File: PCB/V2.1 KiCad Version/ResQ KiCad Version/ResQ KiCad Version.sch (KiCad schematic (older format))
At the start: 8 parts, among them J1 Spare 1, J2 Spare 2, J3 OLED, J4 SD Card, J5 GPS, U1 WeMos_D1_mini

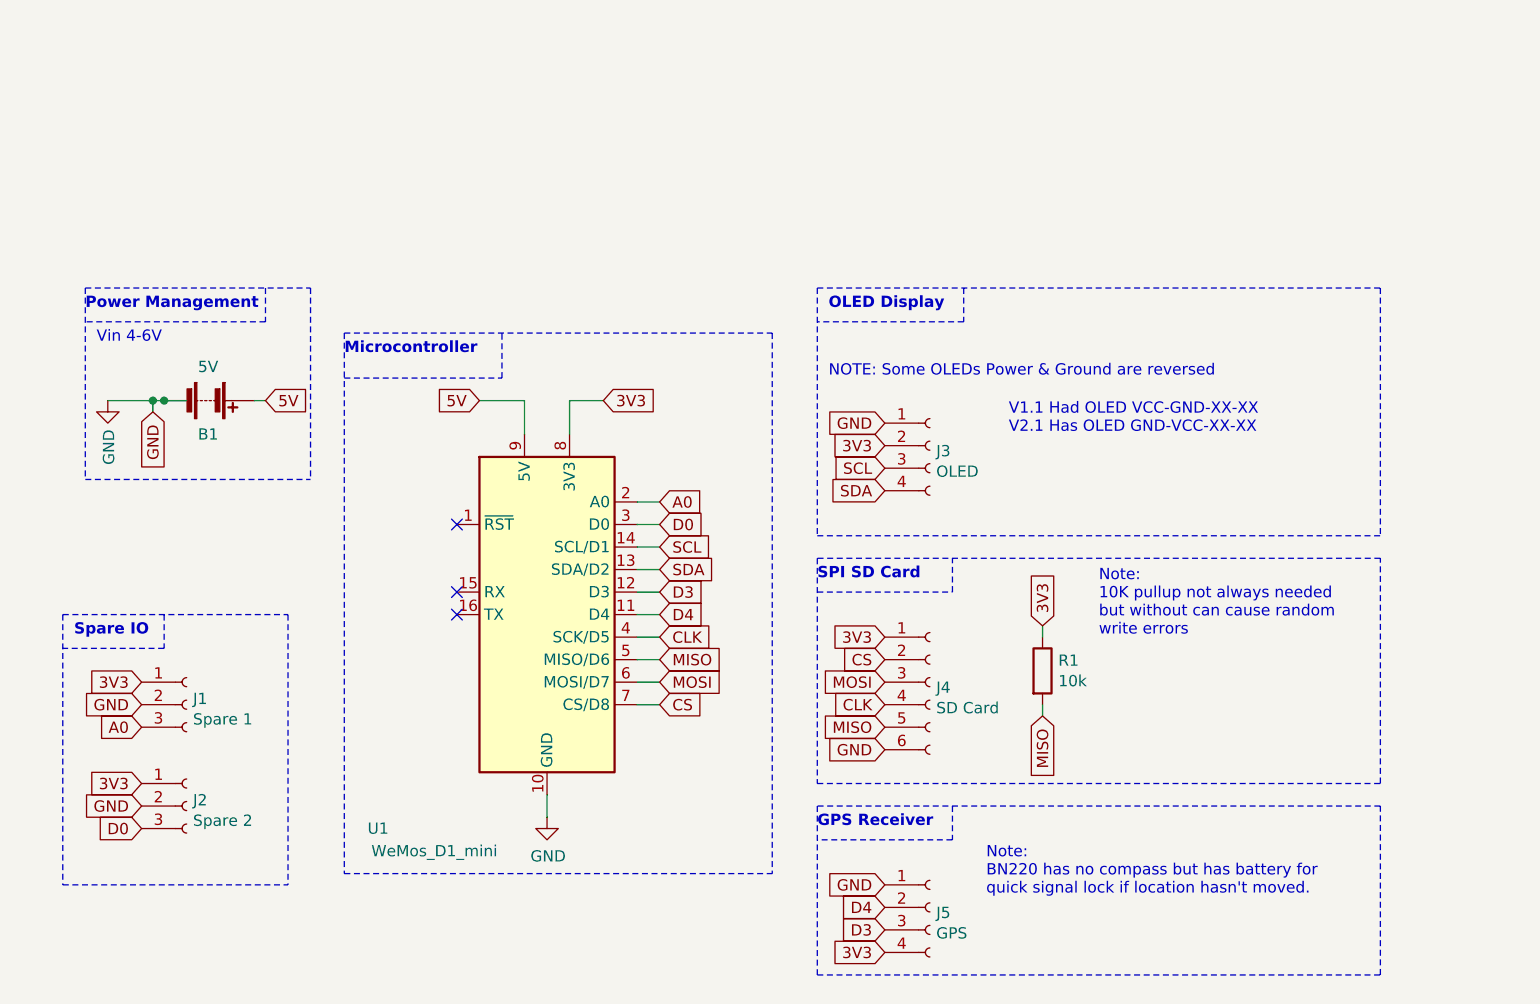
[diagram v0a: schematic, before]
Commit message: Telemetry radio added
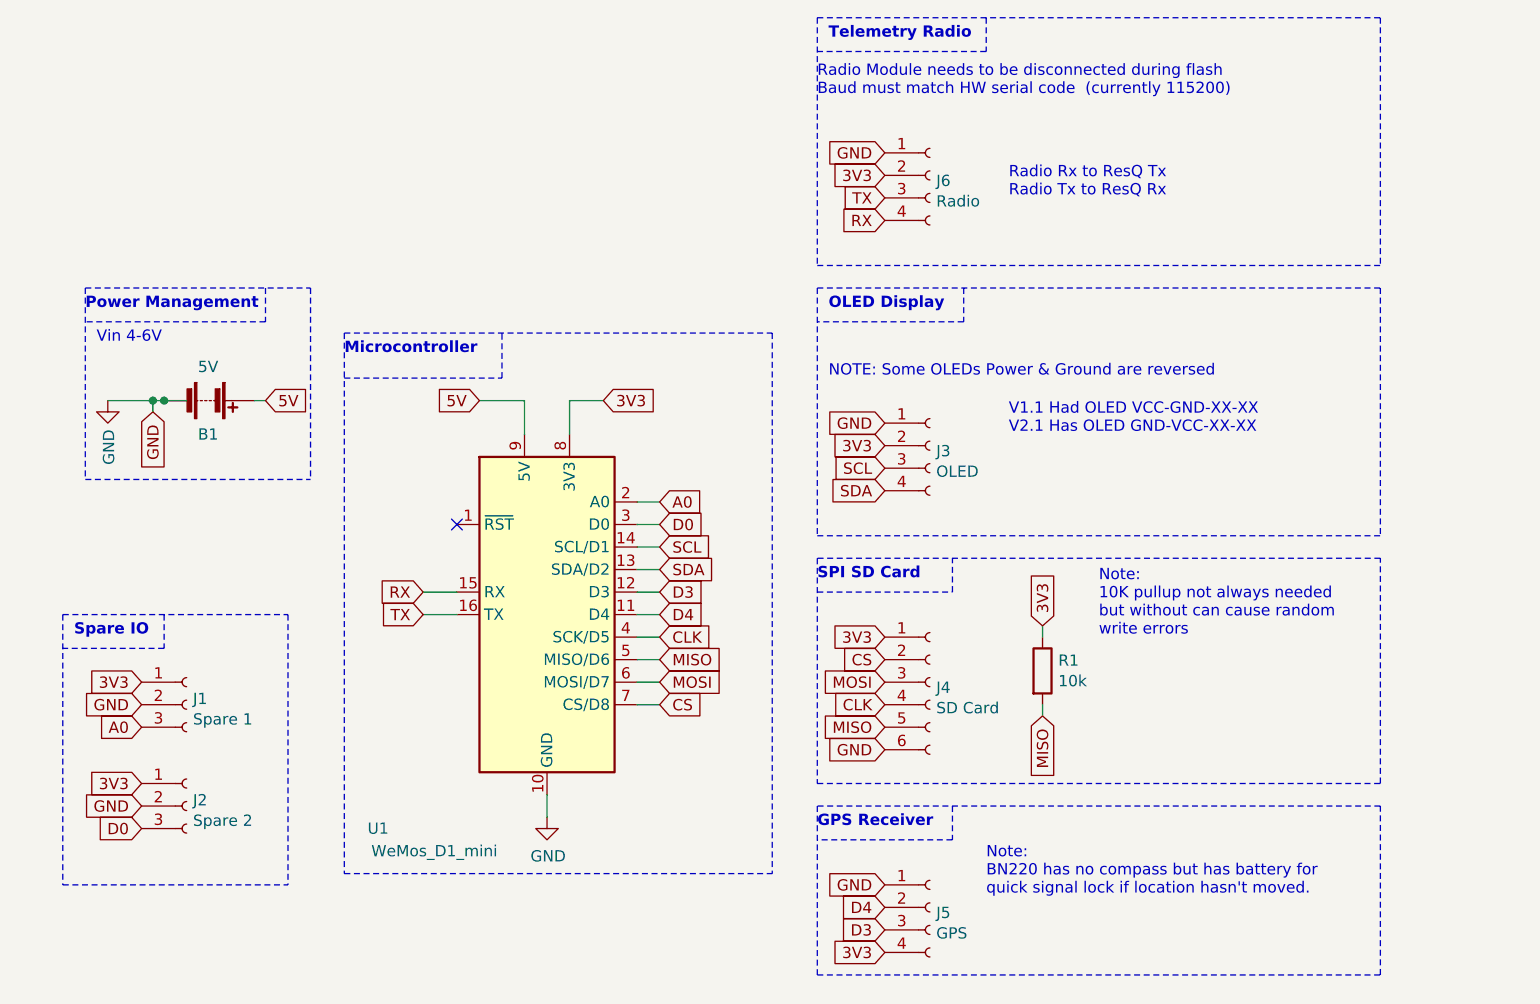
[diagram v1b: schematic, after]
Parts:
- added J6: Radio, Connector_PinSocket_2.54mm:PinSocket_1x04_P2.54mm_Vertical, symbol Connector:Conn_01x04_Female
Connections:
- net labels added: RX, TX
- wire segments 22 -> 24
- no-connect marks 3 -> 1
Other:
- note added: "Radio Module needs to be disconnected during flash \nBaud must match HW serial code (currently 115200)"
- note added: "Radio Rx to ResQ Tx\nRadio Tx to ResQ Rx"
- note added: "Telemetry Radio"
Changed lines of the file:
@@
 Text GLabel 5200 5100 0    50   Input ~ 0
 3V3
-NoConn ~ 6600 4800
-NoConn ~ 6600 4700
 NoConn ~ 6600 4400
 Text GLabel 7500 4700 2    50   Input ~ 0
@@
 	1    0    0    -1
 $EndComp
-Wire Wire Line
-	7000 5600 7000 5700
 Text GLabel 8500 4050 0    50   Input ~ 0
 3V3
@@
 Text Notes 8950 6050 0    50   ~ 0
 Note:\nBN220 has no compass but has battery for \nquick signal lock if location hasn't moved.
-$Comp
-L MCU_Module:WeMos_D1_mini U1
-U 1 1 5F31691B
-P 7000 4800
-F 0 "U1" H 6250 3850 50  0000 C CNN
-F 1 "WeMos_D1_mini" H 6500 3750 50  0000 C CNN
-F 2 "Module:WEMOS_D1_mini_light" H 7000 3650 50  0001 C CNN
-F 3 "https://wiki.wemos.cc/products:d1:d1_mini#documentation" H 5150 3650 50  0001 C CNN
-	1    7000 4800
-	1    0    0    -1
-$EndComp
 Text GLabel 5200 5550 0    50   Input ~ 0
 3V3
@@
 Wire Wire Line
 	7100 3850 7250 3850
+Wire Notes Line
+	8200 2150 8200 3250
+$Comp
+L Connector:Conn_01x04_Female J6
+U 1 1 5F3AE78D
+P 8700 2850
+F 0 "J6" H 8728 2826 50  0000 L CNN
+F 1 "Radio" H 8728 2735 50  0000 L CNN
+F 2 "Connector_PinSocket_2.54mm:PinSocket_1x04_P2.54mm_Vertical" H 8700 2850 50  0001 C CNN
+F 3 "~" H 8700 2850 50  0001 C CNN
+	1    8700 2850
+	1    0    0    -1
+$EndComp
+Text GLabel 8500 2750 0    50   Input ~ 0
+GND
+Text GLabel 8500 2950 0    50   Input ~ 0
+TX
+Text GLabel 8500 3050 0    50   Input ~ 0
+RX
+Text GLabel 8500 2850 0    50   Input ~ 0
+3V3
+Text Notes 8200 2500 0    50   ~ 0
+Radio Module needs to be disconnected during flash \nBaud must match HW serial code  (currently 115200)
+Wire Notes Line
+	10700 2150 10700 3250
+Wire Notes Line
+	8200 2150 10700 2150
+Wire Notes Line
+	8200 3250 10700 3250
+Text Notes 8250 2250 0    50   ~ 10
+Telemetry Radio
+Wire Notes Line
+	8950 2150 8950 2300
+Wire Notes Line
+	8950 2300 8200 2300
+Text GLabel 6450 4800 0    50   Input ~ 0
+TX
+Text GLabel 6450 4700 0    50   Input ~ 0
+RX
+Wire Wire Line
+	7000 5600 7000 5700
+$Comp
+L MCU_Module:WeMos_D1_mini U1
+U 1 1 5F31691B
+P 7000 4800
+F 0 "U1" H 6250 3850 50  0000 C CNN
+F 1 "WeMos_D1_mini" H 6500 3750 50  0000 C CNN
+F 2 "Module:WEMOS_D1_mini_light" H 7000 3650 50  0001 C CNN
+F 3 "https://wiki.wemos.cc/products:d1:d1_mini#documentation" H 5150 3650 50  0001 C CNN
+	1    7000 4800
+	1    0    0    -1
+$EndComp
+Wire Wire Line
+	6600 4700 6450 4700
+Wire Wire Line
+	6600 4800 6450 4800
+Text Notes 9050 2950 0    50   ~ 0
+Radio Rx to ResQ Tx\nRadio Tx to ResQ Rx
 $EndSCHEMATC

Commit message: Scematic fixes
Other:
- note added: "May add switch input\nto allow toggle between menu\nfunctions"
- note added: "Note:\nBN220 has no compass"
- note removed: "Note:\nBN220 has no compass but has battery for \nquick signal lock if location hasn't moved."
- moved on the sheet: B1, J1, J2, J3, J4, J5, J6, R1, U1

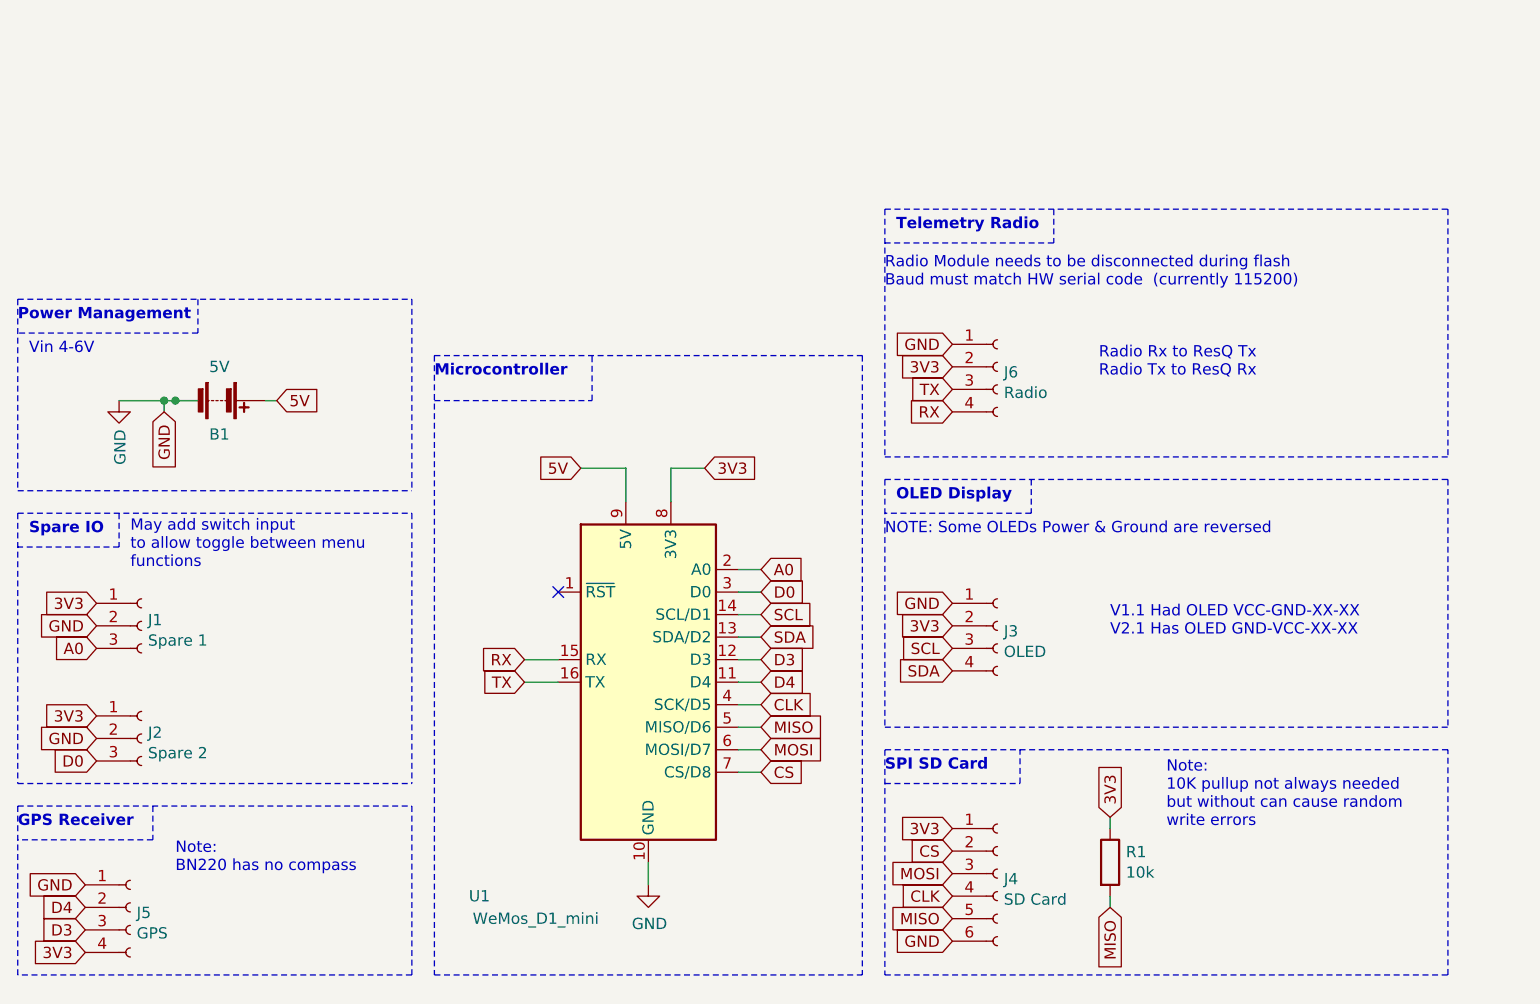
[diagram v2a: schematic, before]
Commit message: Camera Module added
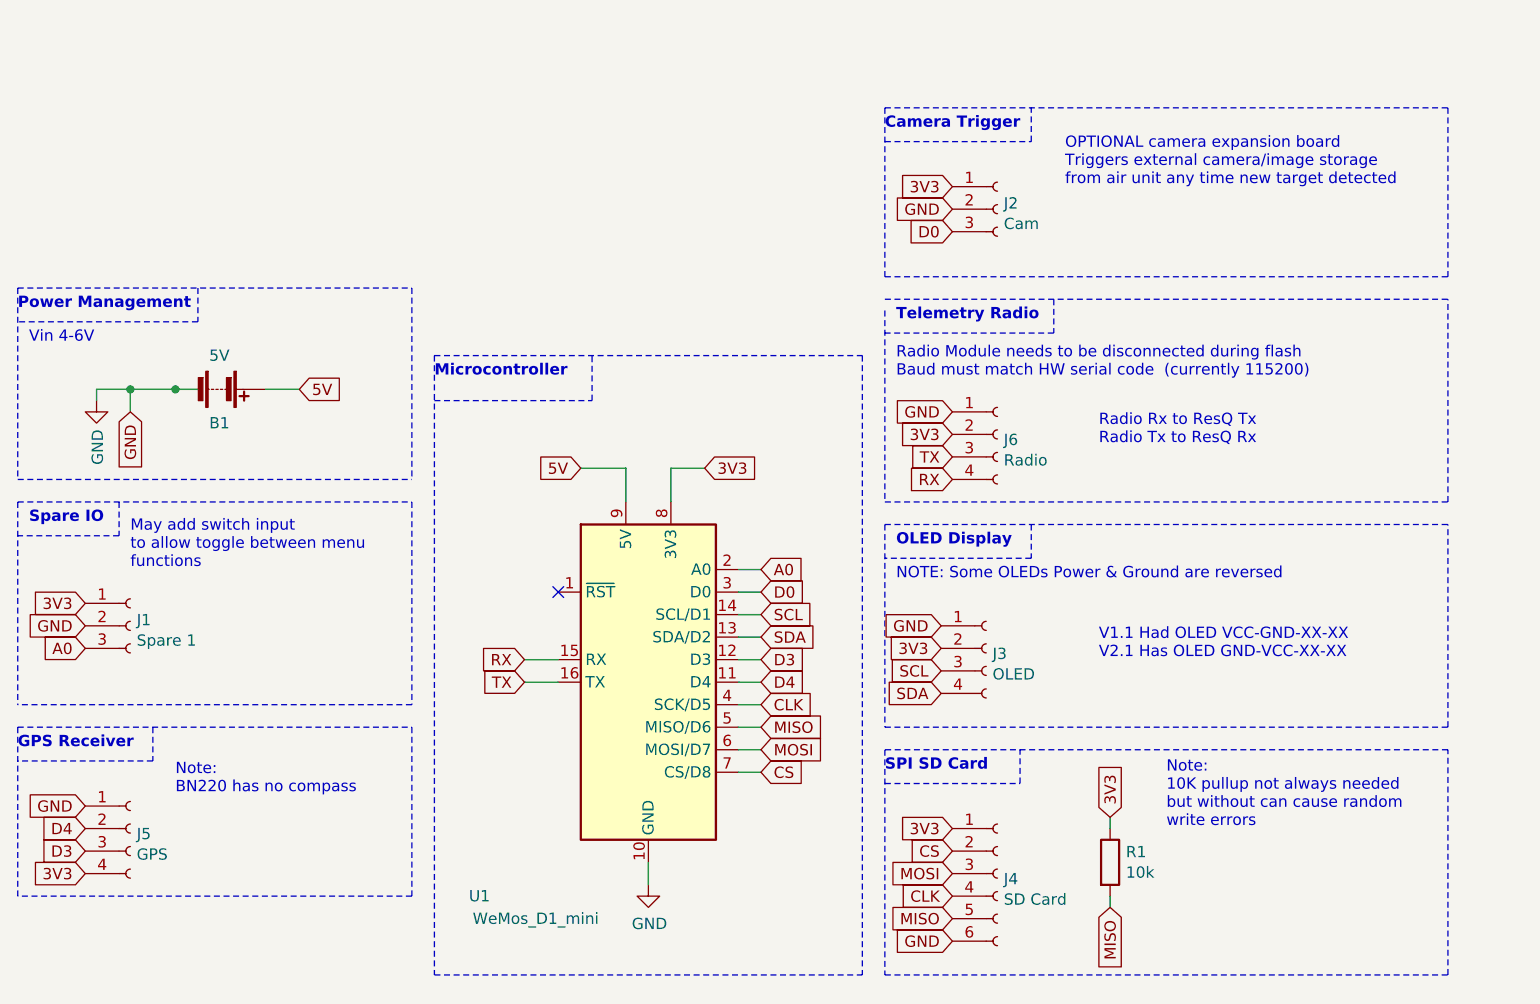
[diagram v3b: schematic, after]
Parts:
- J2: value Spare 2 -> Cam
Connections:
- wire segments 24 -> 25
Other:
- note added: "Camera Trigger\n"
- note added: "OPTIONAL camera expansion board\nTriggers external camera/image storage \nfrom air unit any time new target detected\n"
- moved on the sheet: B1, J1, J2, J3, J5, J6

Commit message: Beginning PCB V2.Xxx Design
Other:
- note added: "Note Layout Changes:\nV1.1 GND-D4-D3-3V3\nV2.xx 3V3-D3-D4-GND\n"
- note added: "V1.1 Had OLED VCC-GND-SCL-SDA\nV2.1 Has OLED GND-VCC-SCL-SDA \n"
- note removed: "Note:\nBN220 has no compass"
- note removed: "V1.1 Had OLED VCC-GND-XX-XX\nV2.1 Has OLED GND-VCC-XX-XX \n"
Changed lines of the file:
@@
 NOTE: Some OLEDs Power & Ground are reversed
 Text Notes 9450 5000 0    50   ~ 0
-V1.1 Had OLED VCC-GND-XX-XX\nV2.1 Has OLED GND-VCC-XX-XX \n
+V1.1 Had OLED VCC-GND-SCL-SDA\nV2.1 Has OLED GND-VCC-SCL-SDA \n
 Wire Notes Line
 	8500 4400 11000 4400
@@
 	1    0    0    -1
 $EndComp
-Text GLabel 8800 3900 0    50   Input ~ 0
-GND
 Text GLabel 8800 4100 0    50   Input ~ 0
 TX
 Text GLabel 8800 4200 0    50   Input ~ 0
 RX
-Text GLabel 8800 4000 0    50   Input ~ 0
-3V3
-Text Notes 8550 3750 0    50   ~ 0
-Radio Module needs to be disconnected during flash \nBaud must match HW serial code  (currently 115200)
+Text GLabel 8800 3900 0    50   Input ~ 0
+3V3
 Wire Notes Line
 	8500 3400 11000 3400
@@
 	4650 5300 6400 5300
 Text Notes 5350 5600 0    50   ~ 0
-Note:\nBN220 has no compass
-Text GLabel 4950 5950 0    50   Input ~ 0
-3V3
-Text GLabel 4950 5650 0    50   Input ~ 0
-GND
+Note Layout Changes:\nV1.1 GND-D4-D3-3V3\nV2.xx 3V3-D3-D4-GND\n
 Wire Notes Line
 	4650 5300 4650 6050
@@
 	1    0    0    -1
 $EndComp
-Text GLabel 4950 5750 0    50   Input ~ 0
-D4
-Text GLabel 4950 5850 0    50   Input ~ 0
-D3
 Text Notes 4650 5400 0    50   ~ 10
 GPS Receiver
@@
 Wire Wire Line
 	5150 3800 5350 3800
+Text Notes 8550 3750 0    50   ~ 0
+Radio Module needs to be disconnected during flash \nBaud must match HW serial code  (currently 115200)
+Text GLabel 8800 4000 0    50   Input ~ 0
+GND
+Text GLabel 4950 5650 0    50   Input ~ 0
+3V3
+Text GLabel 4950 5750 0    50   Input ~ 0
+D3
+Text GLabel 4950 5850 0    50   Input ~ 0
+D4
+Text GLabel 4950 5950 0    50   Input ~ 0
+GND
 $EndSCHEMATC

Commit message: PCB Version 2.1 routed
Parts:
- R1: footprint Resistor_SMD:R_0201_0603Metric -> Resistor_SMD:R_0805_2012Metric_Pad1.15x1.40mm_HandSolder
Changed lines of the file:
@@
 F 0 "R1" H 9570 5946 50  0000 L CNN
 F 1 "10k" H 9570 5855 50  0000 L CNN
-F 2 "Resistor_SMD:R_0201_0603Metric" V 9430 5900 50  0001 C CNN
+F 2 "Resistor_SMD:R_0805_2012Metric_Pad1.15x1.40mm_HandSolder" V 9430 5900 50  0001 C CNN
 F 3 "~" H 9500 5900 50  0001 C CNN
 	1    9500 5900
